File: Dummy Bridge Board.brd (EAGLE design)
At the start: 86.4 x 113.7 mm, 108 parts, among them J2 5787834-1, U14 ADUM3160BRWZ-RL, U16 LM3671MF-3.3/NOPB, U21 CD4050BD, U22 PDS1-S5-S5-M-TR, U28 FT4232HL, U29 SN74HC595DR, U30 LP5907MFX-3.3/NOPB, U49 TL7712A-SOIC, U9 TPS54540DDARQ1, Y2 CX3225GB12000P0HPQCC

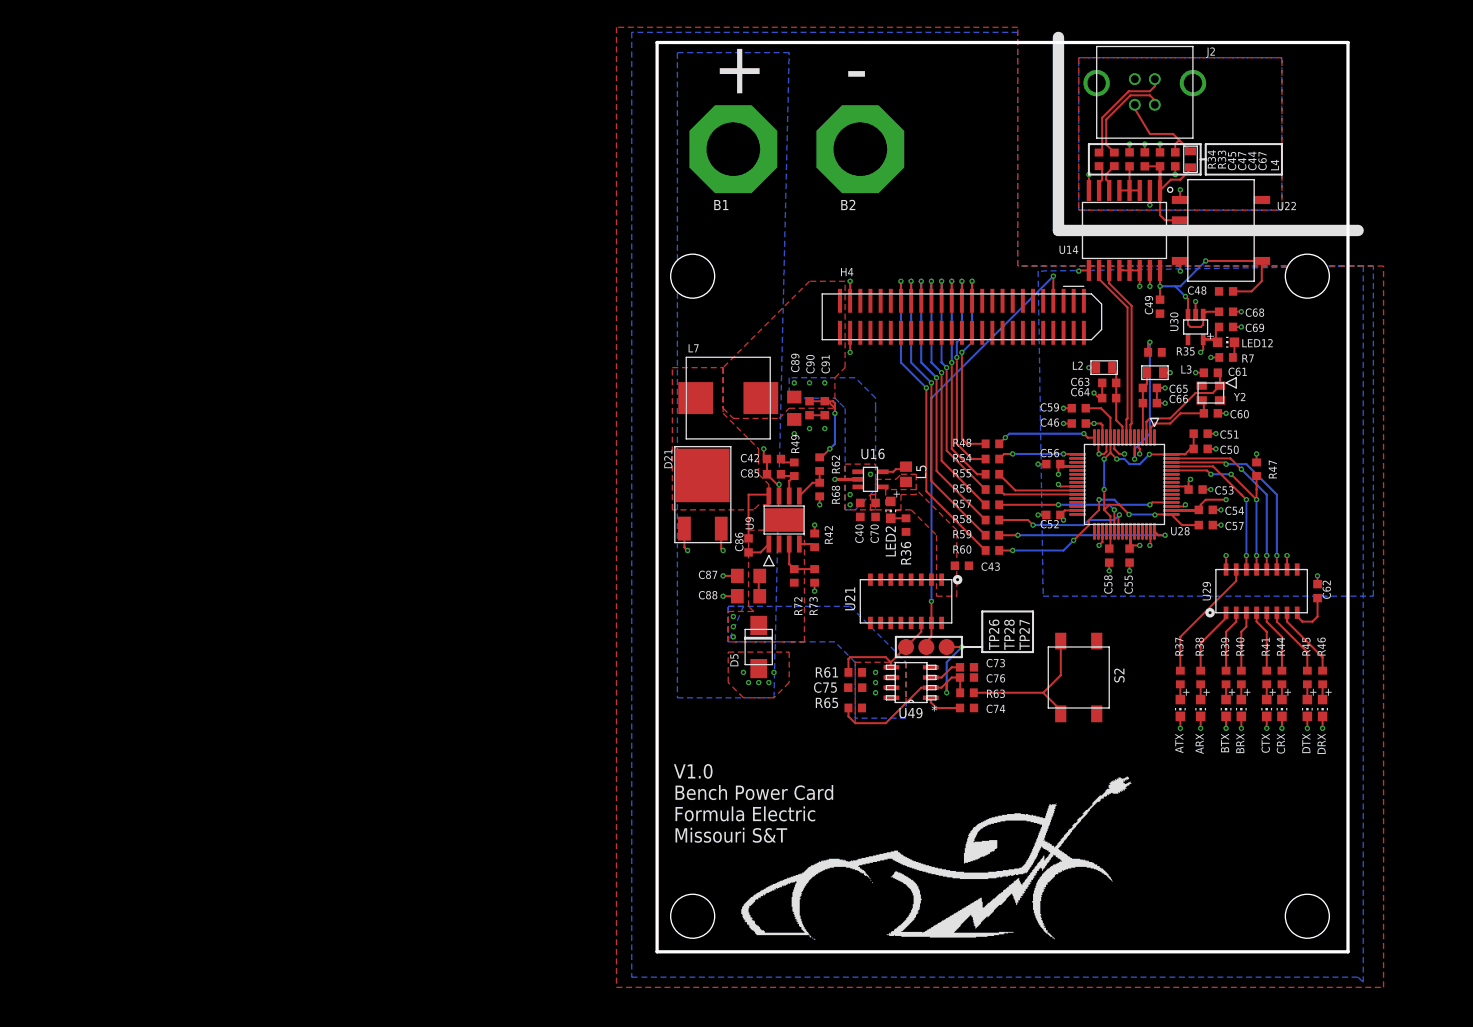
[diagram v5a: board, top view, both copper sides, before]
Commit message: Fixed BOM and made lines all nice and pretty
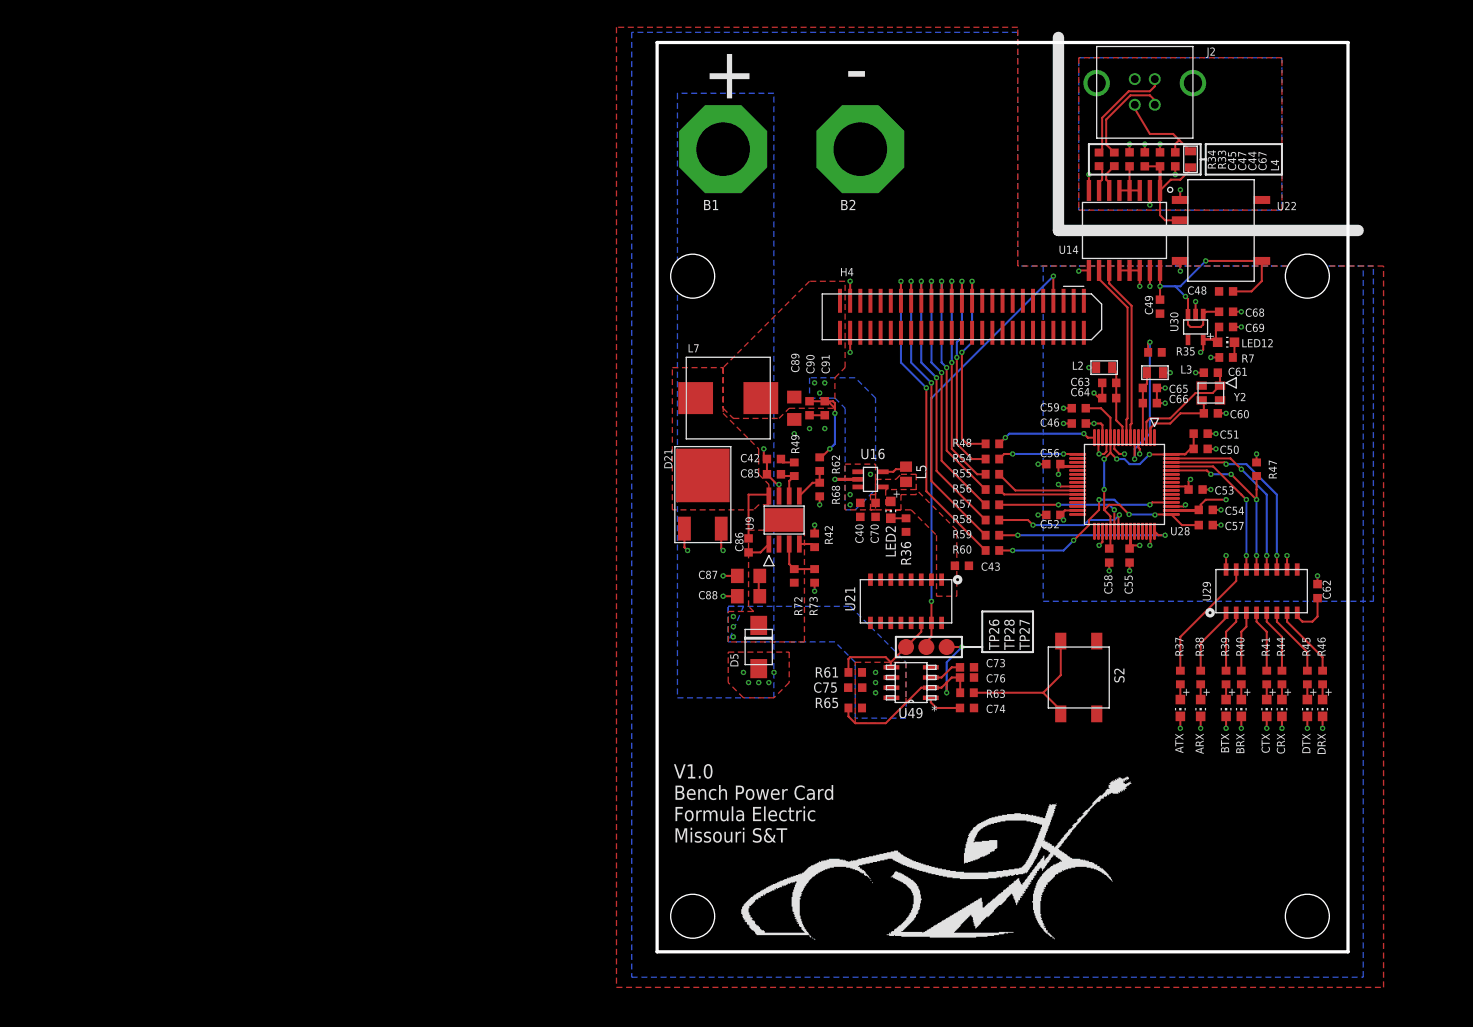
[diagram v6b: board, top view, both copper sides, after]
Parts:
- moved B1 1.27 mm to (8.26, 100.3)
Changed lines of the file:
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@@
 <rectangle x1="58.4708" y1="21.6916" x2="58.9788" y2="21.7932" layer="121"/>
 <rectangle x1="58.674" y1="21.7932" x2="58.8772" y2="21.8948" layer="121"/>
-<text x="6.985" y="107.315" size="6.4516" layer="21">+</text>
+<text x="5.715" y="106.68" size="6.4516" layer="21">+</text>
 <text x="23.495" y="107.315" size="6.4516" layer="21">-</text>
 <wire x1="38.1" y1="38.1" x2="38.1" y2="36.83" width="0.254" layer="21"/>
@@
 <attribute name="PARTNO" value="PMEG3030EP,115" x="12.7" y="31.115" size="1.016" layer="27" rot="R90" display="off"/>
 </element>
-<element name="B1" library="FormE" package="BANANA_SOCKET_VERT" value="BKCT2228-2-ND" x="9.525" y="100.33">
-<attribute name="PARTNO" value="CT2228-2" x="9.525" y="100.33" size="1.778" layer="27" display="off"/>
+<element name="B1" library="FormE" package="BANANA_SOCKET_VERT" value="BKCT2228-2-ND" x="8.255" y="100.33">
+<attribute name="PARTNO" value="CT2228-2" x="8.255" y="100.33" size="1.778" layer="27" display="off"/>
 </element>
 <element name="B2" library="FormE" package="BANANA_SOCKET_VERT" value="BKCT2228-0-ND" x="25.4" y="100.33">
@@
 <vertex x="-3.175" y="114.935"/>
 <vertex x="-3.175" y="-3.175"/>
-<vertex x="87.63" y="-3.175"/>
-<vertex x="88.265" y="-3.81"/>
+<vertex x="88.265" y="-3.175"/>
 <vertex x="88.265" y="85.725"/>
 <vertex x="45.085" y="85.725"/>
@@
 <via x="24.13" y="57.15" extent="1-16" drill="0.3302" diameter="0.254"/>
 <via x="24.13" y="55.88" extent="1-16" drill="0.3302" diameter="0.254"/>
-<via x="17.145" y="71.12" extent="1-16" drill="0.3302" diameter="0.254"/>
-<via x="19.05" y="71.12" extent="1-16" drill="0.3302" diameter="0.254"/>
+<via x="20.32" y="69.85" extent="1-16" drill="0.3302" diameter="0.254"/>
+<via x="19.685" y="71.12" extent="1-16" drill="0.3302" diameter="0.254"/>
 <via x="20.955" y="71.12" extent="1-16" drill="0.3302" diameter="0.254"/>
 <polygon width="0.254" layer="16">
-<vertex x="17.145" y="69.215"/>
+<vertex x="19.05" y="69.215"/>
 <vertex x="22.225" y="69.215"/>
-<vertex x="22.86" y="68.58"/>
 <vertex x="23.495" y="67.945"/>
 <vertex x="23.495" y="55.245"/>
 <vertex x="24.765" y="55.245"/>
 <vertex x="27.305" y="57.785"/>
-<vertex x="27.305" y="67.945"/>
 <vertex x="27.305" y="69.215"/>
 <vertex x="24.765" y="71.755"/>
-<vertex x="16.51" y="71.755"/>
-<vertex x="16.51" y="69.215"/>
+<vertex x="19.05" y="71.755"/>
 </polygon>
 </signal>
@@
 <polygon width="0.254" layer="16" rank="2">
 <vertex x="89.535" y="85.725"/>
-<vertex x="47.625" y="85.09"/>
-<vertex x="48.26" y="44.45"/>
-<vertex x="89.535" y="44.45"/>
+<vertex x="48.26" y="85.725"/>
+<vertex x="48.26" y="43.815"/>
+<vertex x="89.535" y="43.815"/>
 </polygon>
 <wire x1="52.57" y1="60.67" x2="50.455" y2="60.67" width="0.254" layer="1"/>
@@
 <contactref element="D5" pad="ANODE"/>
 <polygon width="0.254" layer="16">
-<vertex x="16.51" y="112.395"/>
-<vertex x="2.54" y="112.395"/>
+<vertex x="14.605" y="107.315"/>
+<vertex x="2.54" y="107.315"/>
 <vertex x="2.54" y="31.75"/>
 <vertex x="14.605" y="31.75"/>
